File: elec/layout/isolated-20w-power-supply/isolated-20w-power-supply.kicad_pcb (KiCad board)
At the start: 2 copper layers, 9 parts

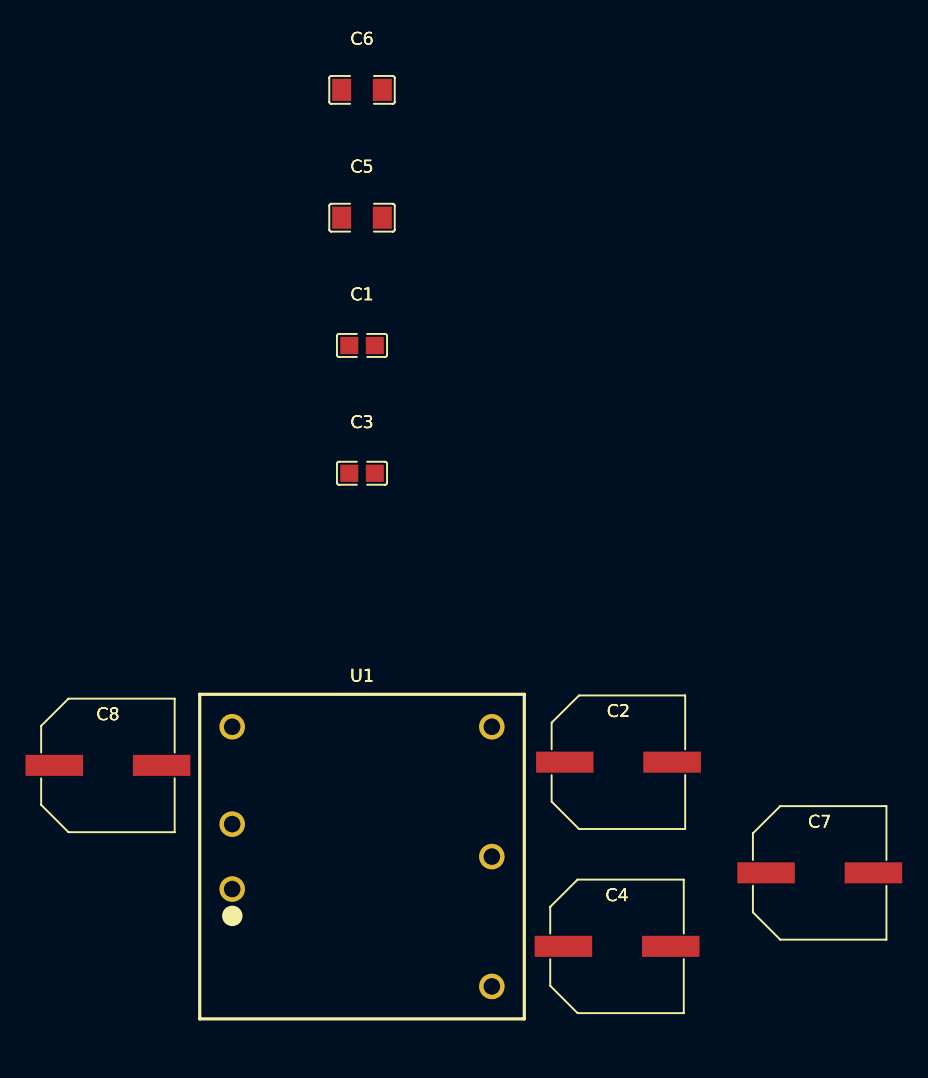
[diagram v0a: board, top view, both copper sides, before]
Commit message: route 20W supply
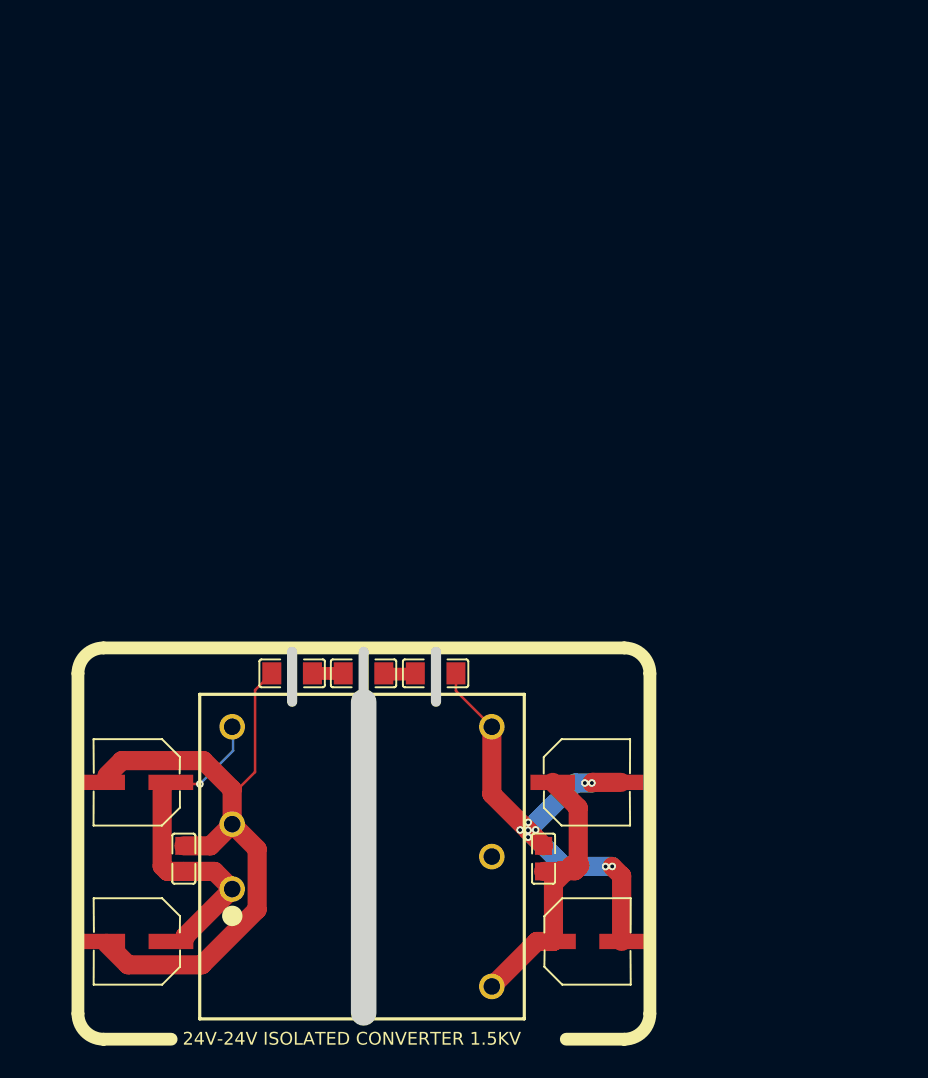
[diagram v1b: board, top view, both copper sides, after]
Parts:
- added C9: 2.2nF ±10% 1kV X7R, atopile:C1206-f0a137, F.Cu at (102.4, 84.7)
- C2, C4, C7, C8: value (none) -> 100µF ±20%; footprint atopile:CAP-SMD_BD10.0-L10.3-W10.3-LS11.6-FD-b102ff -> atopile:CAP-SMD_BD6.3-L6.6-W6.6-FD-3e301d
- moved C7 53.9 mm to (79.0, 93.2), turned to 180 degrees
- moved C6 45.7 mm to (96.8, 84.7)
- moved C1 42.5 mm to (82.7, 99.2), turned to 90 degrees
- moved C2 40.2 mm to (79.0, 105.7), turned to 180 degrees
- moved C8 37.5 mm to (114.2, 93.2)
- moved C5 36.1 mm to (91.2, 84.7)
- moved C3 33.3 mm to (110.8, 99.2), turned to 90 degrees
- moved C4 2.34 mm to (114.3, 105.7)
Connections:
- C1 pad 1: anode-1 -> hv-1
- C1 pad 2: gnd -> gnd-1
- C2 pad 1: anode-1 -> hv-1
- C2 pad 2: input_cap_2-net -> gnd-1
- C3 pad 1: anode -> hv
- C3 pad 2: gnd-1 -> gnd
- C4 pad 1: anode -> hv
- C4 pad 2: output_cap_2-net -> gnd
- C5 pad 1: gnd -> gnd-1
- C6 pad 2: gnd -> net-1
- C7 pad 1: anode-1 -> hv-1
- C7 pad 2: input_cap_3-net -> gnd-1
- C8 pad 1: anode -> hv
- C8 pad 2: output_cap_3-net -> gnd
- U1 pad 1: VINplus -> hv-1
- U1 pad 2: converter-gnd -> gnd-1
- U1 pad 3: CNT -> hv-1
- U1 pad 4: converter-gnd-1 -> gnd
- U1 pad 6: VOplus -> hv
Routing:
- net gnd-1: track 0.00 -> 54.3 mm
- net gnd: track 0.00 -> 39.1 mm, vias 0 -> 9
- net hv-1: track 0.00 -> 27.5 mm, vias 0 -> 1
- net hv: track 0.00 -> 24.0 mm
- net net-1: track 0.00 -> 2.48 mm
- net net: track 0.00 -> 2.41 mm
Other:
- board outline added: 11.3 x 28.3 mm
- board text added: "24V-24V ISOLATED CONVERTER 1.5KV"

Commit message: Layout updated
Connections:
- C1 pad 1: hv-1 -> hv
- C1 pad 2: gnd-1 -> gnd
- C2 pad 1: hv-1 -> hv
- C2 pad 2: gnd-1 -> gnd
- C3 pad 1: hv -> hv-1
- C3 pad 2: gnd -> gnd-1
- C4 pad 1: hv -> hv-1
- C4 pad 2: gnd -> gnd-1
- C5 pad 1: gnd-1 -> gnd
- C5 pad 2: net -> net-1
- C6 pad 1: net -> net-1
- C6 pad 2: net-1 -> net
- C7 pad 1: hv-1 -> hv
- C7 pad 2: gnd-1 -> gnd
- C8 pad 1: hv -> hv-1
- C8 pad 2: gnd -> gnd-1
- C9 pad 1: net-1 -> net
- C9 pad 2: gnd -> gnd-1
- U1 pad 1: hv-1 -> hv
- U1 pad 2: gnd-1 -> gnd
- U1 pad 3: hv-1 -> hv
- U1 pad 4: gnd -> gnd-1
- U1 pad 6: hv -> hv-1
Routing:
- net gnd-1: track 54.3 -> 39.1 mm, vias 0 -> 9
- net gnd: track 39.1 -> 54.3 mm, vias 9 -> 0
- net hv-1: track 27.5 -> 24.0 mm, vias 1 -> 0
- net hv: track 24.0 -> 27.5 mm, vias 0 -> 1

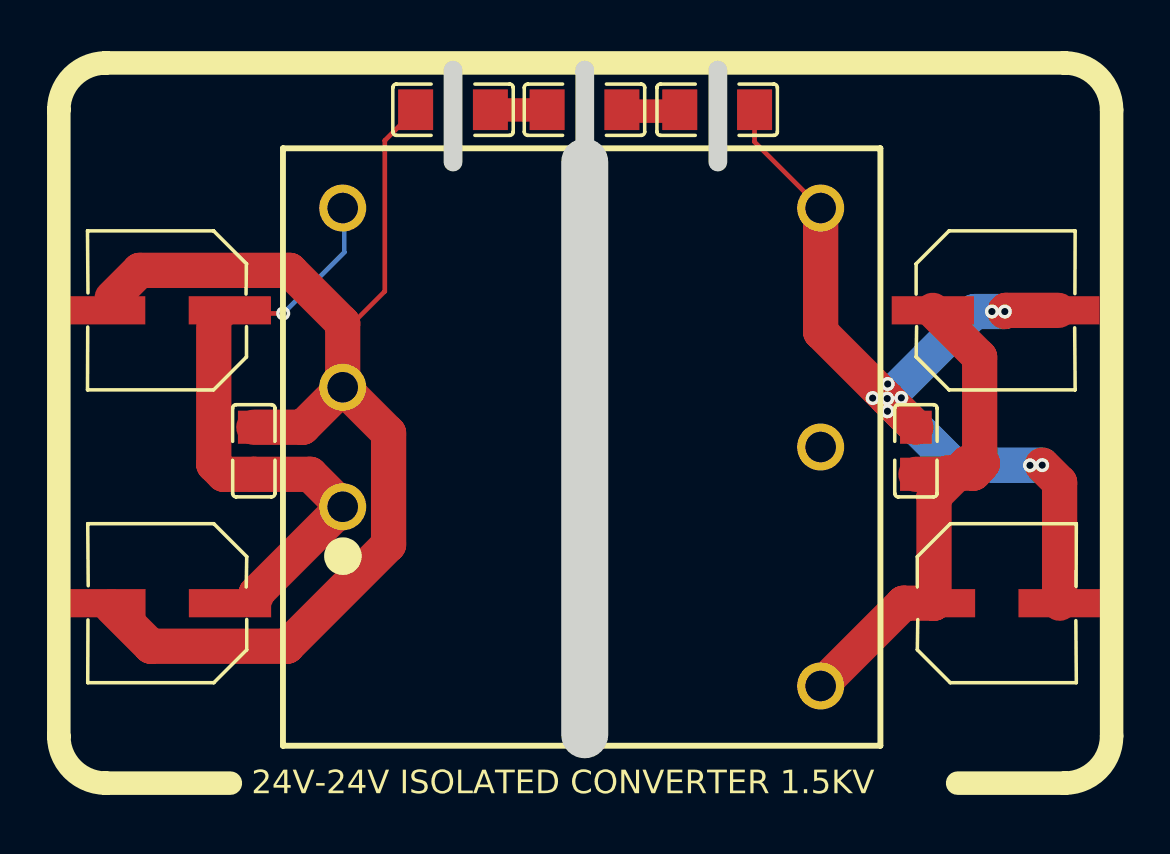
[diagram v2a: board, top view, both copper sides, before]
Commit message: remove vendored tca9548a, make thermistor 8ch block, make saleae debug header layout
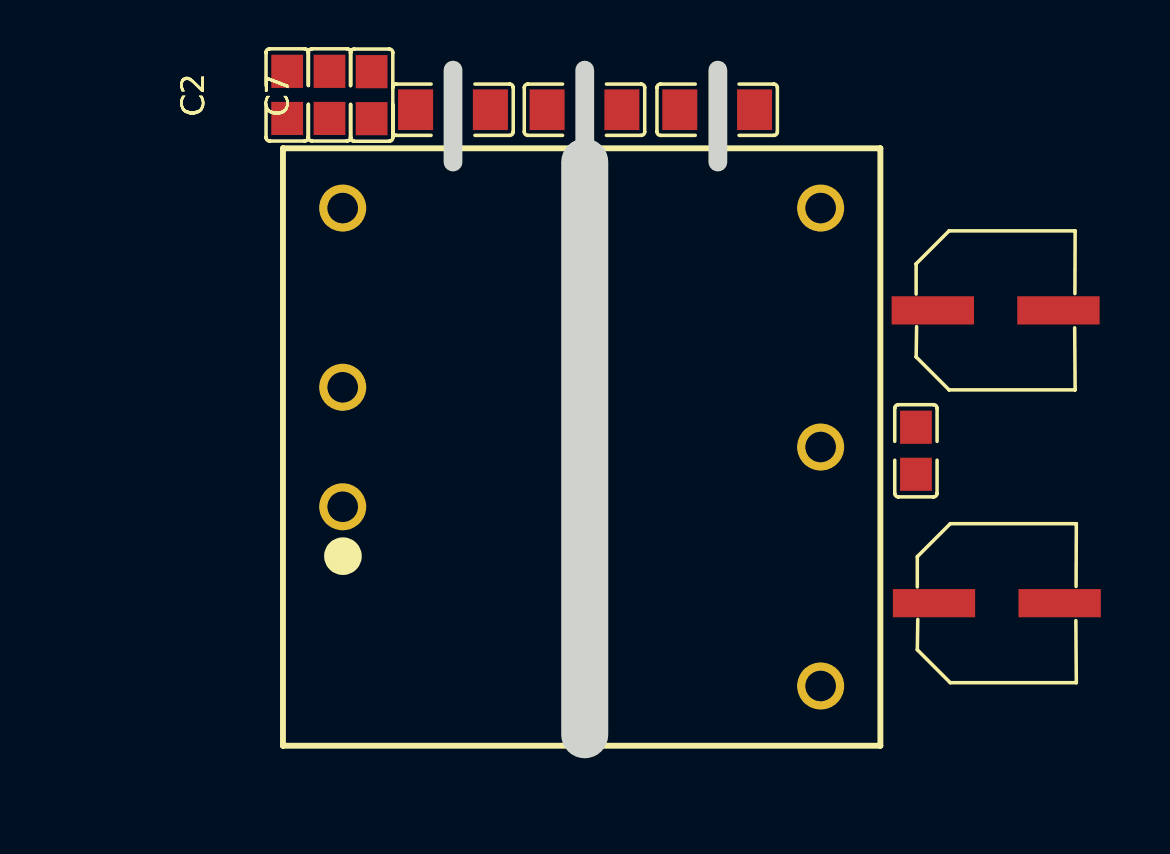
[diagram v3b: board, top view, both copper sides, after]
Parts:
- C1: value 1µF ±10% 50V X7R -> 10µF ±10% 50V X5R
- C2: value 100µF ±20% -> 10µF ±10% 50V X5R; footprint atopile:CAP-SMD_BD6.3-L6.6-W6.6-FD-3e301d -> atopile:C0805-3b2e55
- C5, C6, C9: value 2.2nF ±10% 1kV X7R -> 2.2nF ±5% 1kV C0G
- C7: value 100µF ±20% -> 1µF ±10% 50V X7R; footprint atopile:CAP-SMD_BD6.3-L6.6-W6.6-FD-3e301d -> atopile:C0805-3b2e55
- moved C2 22.2 mm to (84.1, 84.1), turned to 90 degrees
- moved C1 15.5 mm to (85.9, 84.1)
- moved C7 12.6 mm to (87.7, 84.1), turned to 90 degrees
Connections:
- C1 pad 1: hv -> hv-1
- C2 pad 1: hv -> hv-1
- C3 pad 1: hv-1 -> hv
- C4 pad 1: hv-1 -> hv
- C7 pad 1: hv -> hv-1
- C8 pad 1: hv-1 -> hv
- U1 pad 1: hv -> hv-1
- U1 pad 3: hv -> hv-1
- U1 pad 6: hv-1 -> hv
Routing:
- net gnd: track 54.3 -> 0.00 mm
- net gnd-1: track 39.1 -> 0.00 mm, vias 9 -> 0
- net hv: track 27.5 -> 0.00 mm, vias 1 -> 0
- net hv-1: track 24.0 -> 0.00 mm
- net net: track 2.48 -> 0.00 mm
- net net-1: track 2.41 -> 0.00 mm
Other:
- board text removed: "24V-24V ISOLATED CONVERTER 1.5KV"

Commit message: building frozen
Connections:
- C1 pad 2: gnd -> gnd-1
- C2 pad 2: gnd -> gnd-1
- C3 pad 2: gnd-1 -> gnd
- C4 pad 2: gnd-1 -> gnd
- C5 pad 1: gnd -> gnd-1
- C7 pad 2: gnd -> gnd-1
- C8 pad 2: gnd-1 -> gnd
- C9 pad 2: gnd-1 -> gnd
- U1 pad 2: gnd -> gnd-1
- U1 pad 4: gnd-1 -> gnd

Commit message: building locally to fix frozen builds
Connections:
- C1 pad 1: hv-1 -> hv
- C2 pad 1: hv-1 -> hv
- C3 pad 1: hv -> hv-1
- C4 pad 1: hv -> hv-1
- C5 pad 2: net-1 -> net
- C6 pad 1: net-1 -> net
- C6 pad 2: net -> net-1
- C7 pad 1: hv-1 -> hv
- C8 pad 1: hv -> hv-1
- C9 pad 1: net -> net-1
- U1 pad 1: hv-1 -> hv
- U1 pad 3: hv-1 -> hv
- U1 pad 6: hv -> hv-1
